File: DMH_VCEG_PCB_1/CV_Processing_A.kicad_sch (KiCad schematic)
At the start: 58 parts, among them J22 Conn_01x10_PinHeader, Q11 BC558, Q12 BC558, Q13 BC548, Q14 BC548, Q15 BC548, Q16 BC548, U10 TL074, U8 TL074, U9 TL074

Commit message: PCB 2 routing in progress
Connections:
- net Att CV: now also J22.5 (Pin_5)
- net Dec CV: now also J22.6 (Pin_6)
- net Rel CV: now also J22.8 (Pin_8)
- net Sus CV: now also J22.7 (Pin_7)
- no-connect marks 4 -> 0
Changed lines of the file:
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@@
+	)
+	(junction
+		(at 33.02 139.7)
+		(diameter 0)
+		(color 0 0 0 0)
 	)
 	(junction
@@
 	)
 	(junction
+		(at 45.72 185.42)
+		(diameter 0)
+		(color 0 0 0 0)
+	)
+	(junction
 		(at 127 49.53)
 		(diameter 0)
@@
 	)
 	(junction
+		(at 45.72 19.05)
+		(diameter 0)
+		(color 0 0 0 0)
+	)
+	(junction
 		(at 167.64 224.79)
 		(diameter 0)
@@
 	)
 	(junction
+		(at 45.72 76.2)
+		(diameter 0)
+		(color 0 0 0 0)
+	)
+	(junction
 		(at 158.75 218.44)
 		(diameter 0)
@@
 		(color 0 0 0 0)
 	)
-	(no_connect
-		(at 33.02 137.16)
-	)
-	(no_connect
-		(at 48.26 76.2)
-	)
-	(no_connect
-		(at 48.26 19.05)
-	)
-	(no_connect
-		(at 48.26 185.42)
-	)
 	(wire
 		(pts
@@
 	(wire
 		(pts
+			(xy 45.72 185.42) (xy 48.26 185.42)
+		)
+		(stroke
+			(width 0)
+			(type default)
+		)
+	)
+	(wire
+		(pts
 			(xy 118.11 69.85) (xy 116.84 69.85)
 		)
@@
 	(wire
 		(pts
+			(xy 45.72 76.2) (xy 48.26 76.2)
+		)
+		(stroke
+			(width 0)
+			(type default)
+		)
+	)
+	(wire
+		(pts
 			(xy 49.53 106.68) (xy 45.72 106.68)
 		)
@@
 	(wire
 		(pts
+			(xy 45.72 19.05) (xy 48.26 19.05)
+		)
+		(stroke
+			(width 0)
+			(type default)
+		)
+	)
+	(wire
+		(pts
 			(xy 83.82 91.44) (xy 83.82 104.14)
 		)
@@
 	(wire
 		(pts
+			(xy 33.02 139.7) (xy 35.56 139.7)
+		)
+		(stroke
+			(width 0)
+			(type default)
+		)
+	)
+	(wire
+		(pts
 			(xy 96.52 137.16) (xy 93.98 137.16)
 		)
@@
 	(wire
 		(pts
+			(xy 33.02 137.16) (xy 33.02 139.7)
+		)
+		(stroke
+			(width 0)
+			(type default)
+		)
+	)
+	(wire
+		(pts
 			(xy 83.82 46.99) (xy 87.63 46.99)
 		)
@@
 	(wire
 		(pts
-			(xy 30.48 139.7) (xy 35.56 139.7)
-		)
-		(stroke
+			(xy 30.48 139.7) (xy 33.02 139.7)
+		)
+		(stroke

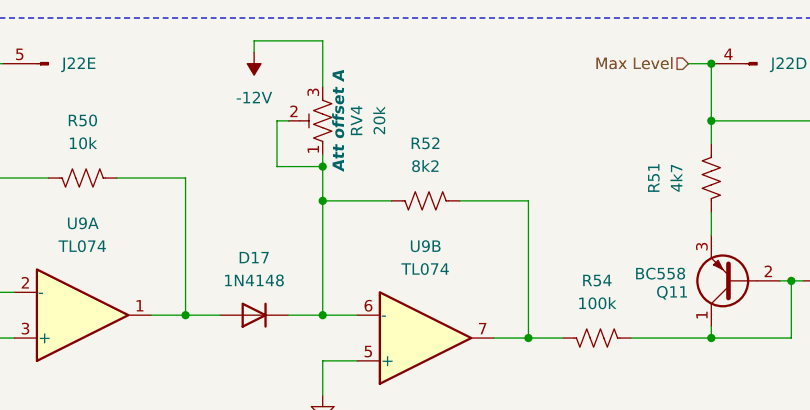
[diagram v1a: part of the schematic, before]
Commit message: Found better calib value for attack
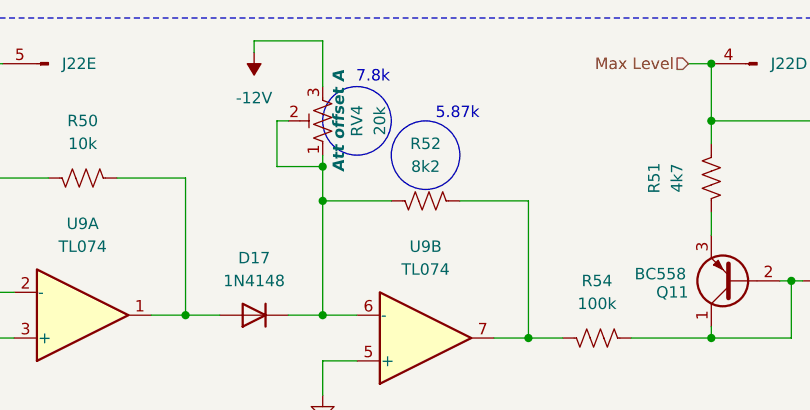
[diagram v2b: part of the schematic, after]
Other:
- note added: "5.87k"
- note added: "7.8k"
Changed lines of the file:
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@@
+		)
+	)
+	(circle
+		(center 95.25 29.21)
+		(radius 3.81)
+		(stroke
+			(width 0)
+			(type default)
+		)
+		(fill
+			(type none)
+		)
+	)
+	(circle
+		(center 87.63 25.4)
+		(radius 3.81)
+		(stroke
+			(width 0)
+			(type default)
+		)
+		(fill
+			(type none)
 		)
 	)
@@
 		(effects
 			(font
+				(size 1.27 1.27)
+			)
+		)
+	)
+	(text "7.8k"
+		(exclude_from_sim no)
+		(at 89.408 20.574 0)
+		(effects
+			(font
+				(size 1.27 1.27)
+			)
+		)
+	)
+	(text "5.87k"
+		(exclude_from_sim no)
+		(at 98.806 24.638 0)
+		(effects
+			(font
